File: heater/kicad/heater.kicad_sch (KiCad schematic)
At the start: 78 parts, among them J1 Conn_01x02_Pin, J2 Conn_01x02_Pin, J5 pcie_98, U1 OPA863DBVR, U10 B0509XT-1WR3, U14 OPA863DBVR, U15 LTC1968, U16 OPA863DBVR, U2 ESD5344D-TP, U4 TPS7A2050PDBVR, U5 ISO1541, U6 LTC1968, U7 OPA863DBVR, U8 ADS1115IDGS, U9 XC6206P332MR

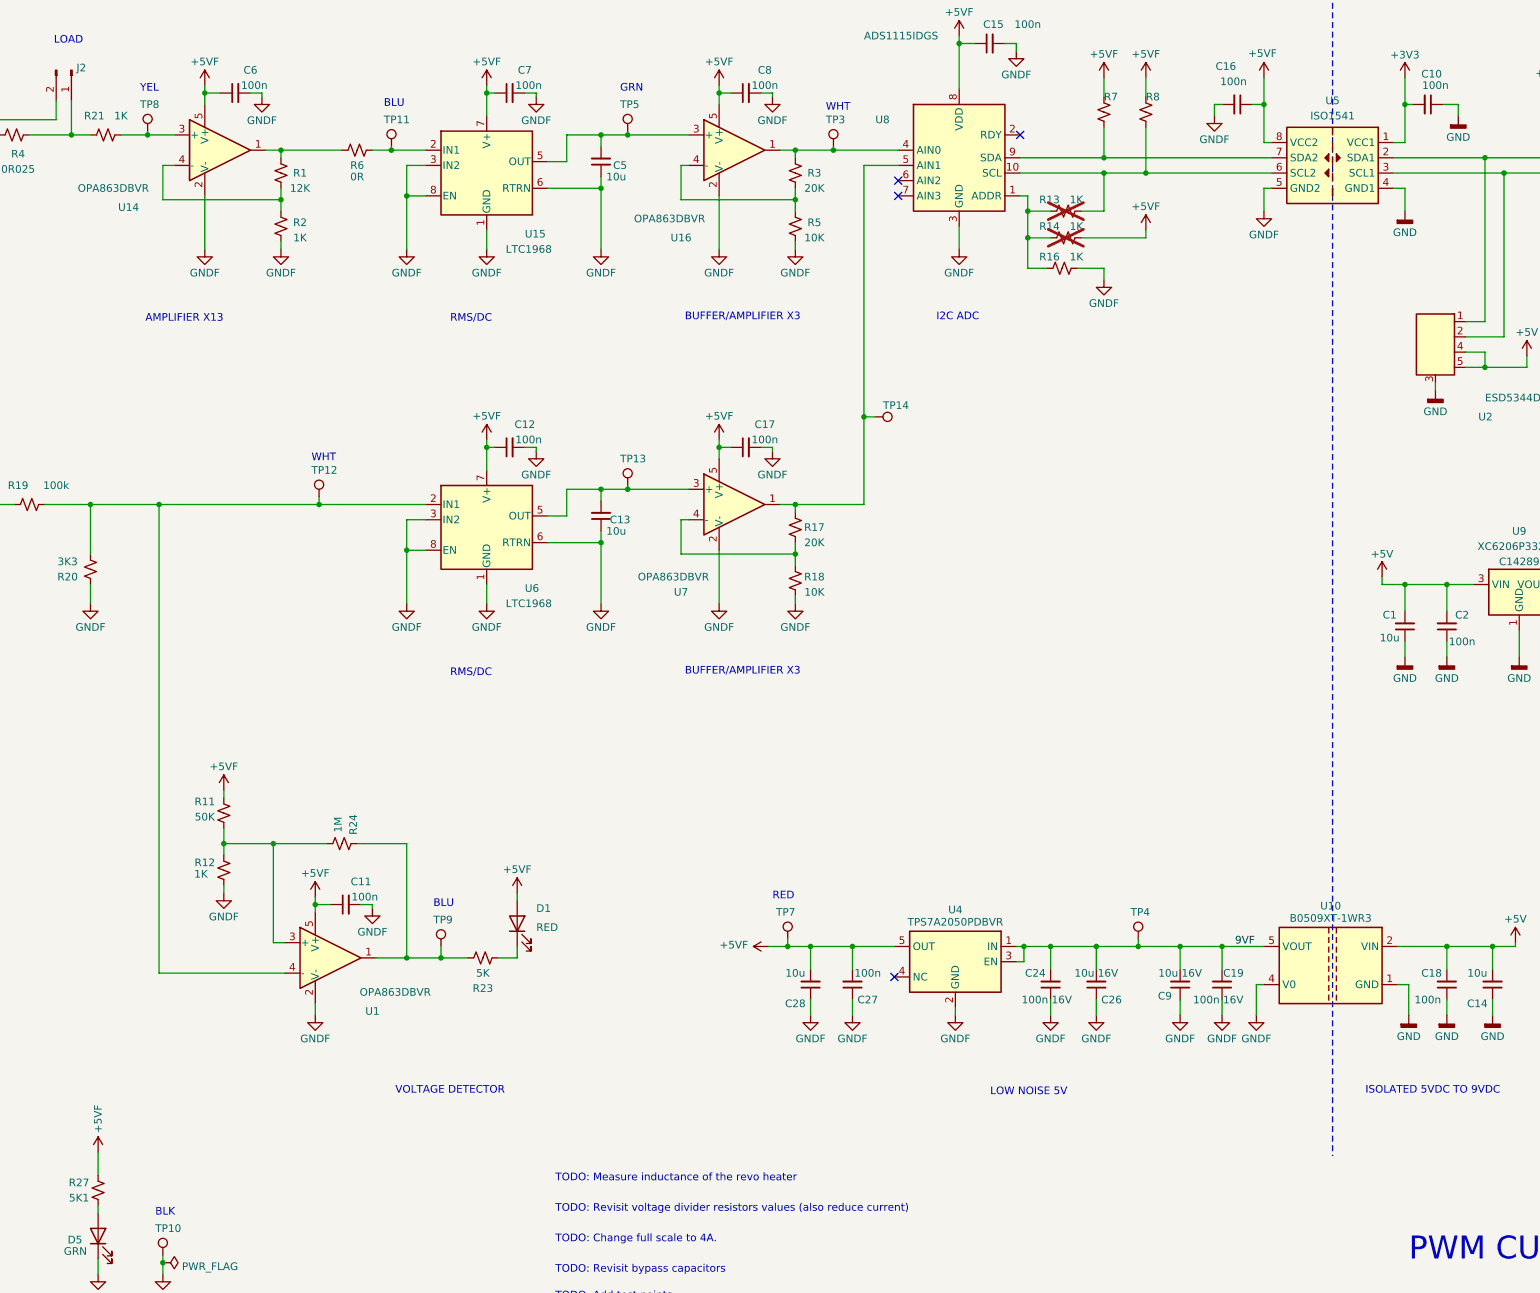
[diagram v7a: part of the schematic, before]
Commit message: Updated heater schematic.
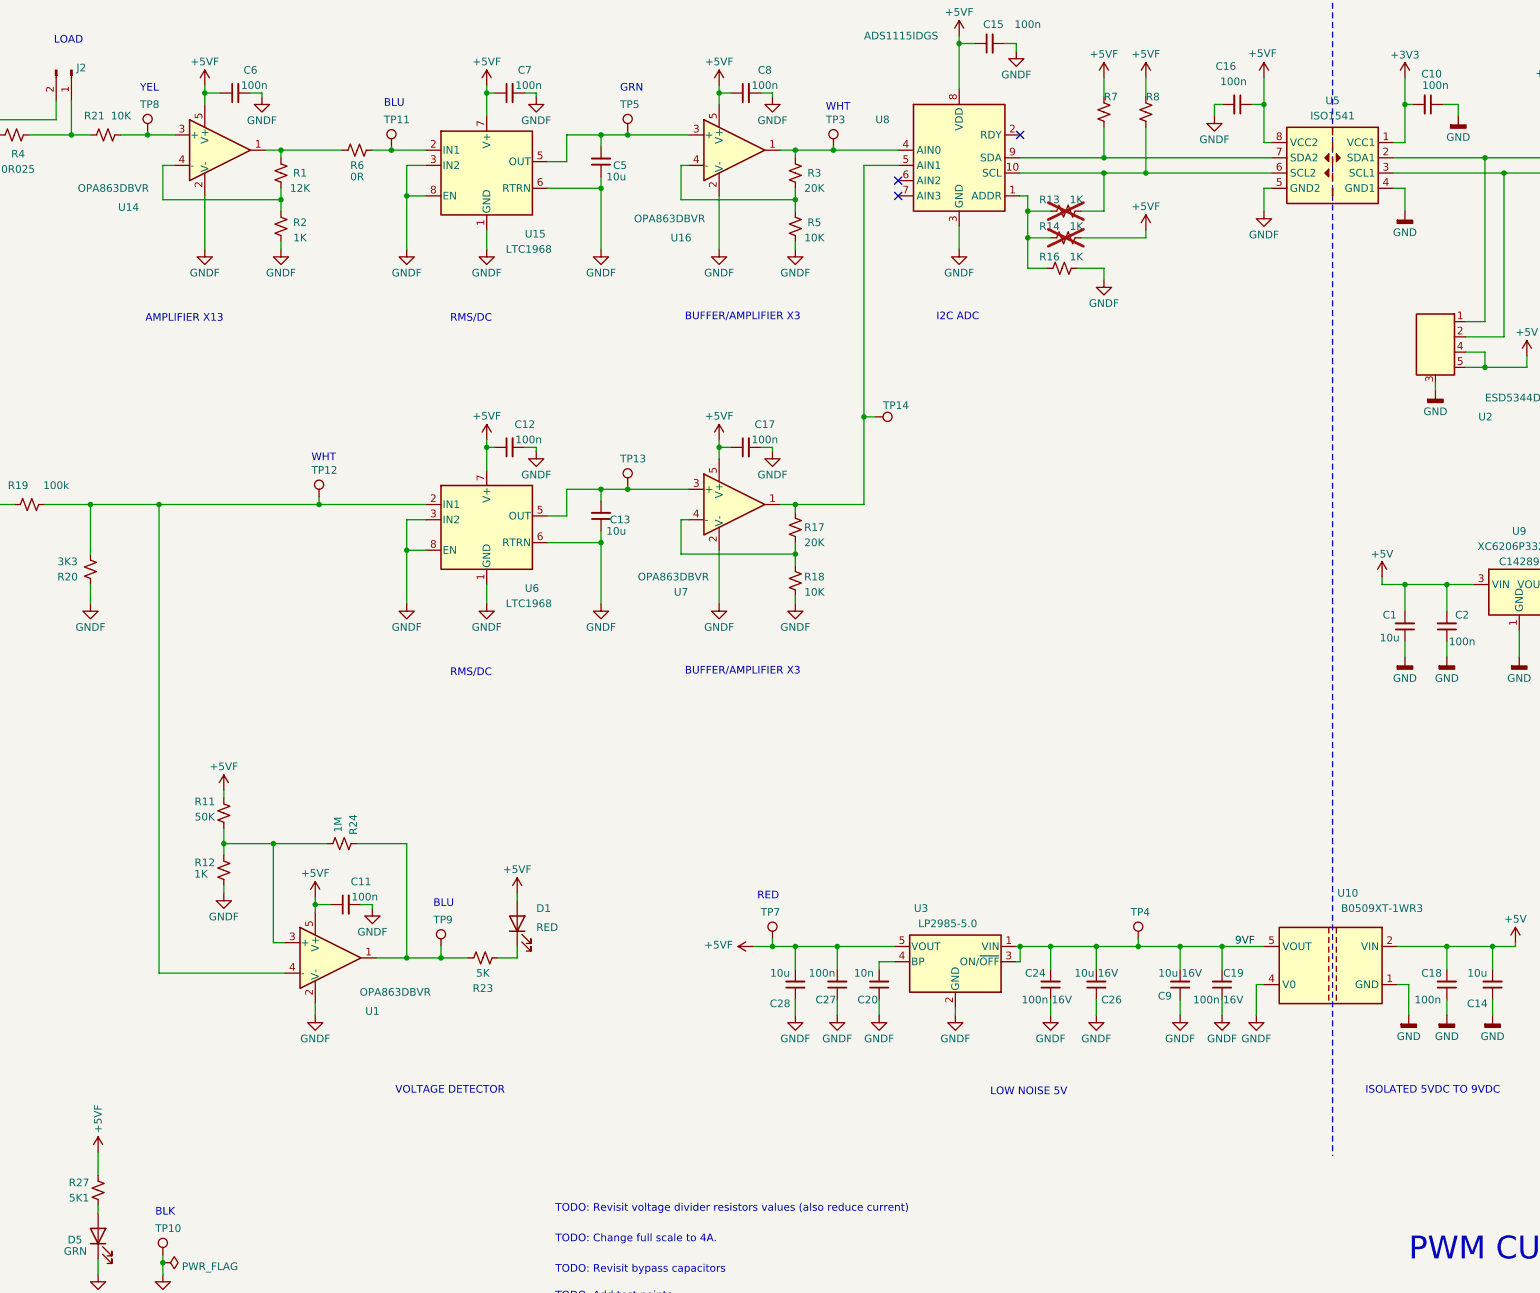
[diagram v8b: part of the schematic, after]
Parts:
- removed U4: TPS7A2050PDBVR, heater:SOT-23-5, symbol heater:TPS7A2050
- added C20: 10n, Capacitor_SMD:C_0402_1005Metric, symbol Device:C_Small
- added U3: LP2985-5.0, Package_TO_SOT_SMD:SOT-23-5, symbol Regulator_Linear:LP2985-5.0
- R21: value 1K -> 10K; LCSC C11702 -> (none)
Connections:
- net +5VF: now also U3.5 (VOUT)
- net 9VF: now also U3.1 (VIN), U3.3 (ON/~{OFF})
- net GND1: now also C20.1, U3.2 (GND)
- new net: C20.2, U3.4 (BP)
- no-connect marks 92 -> 91
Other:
- note removed: "TODO: Measure inductance of the revo heater"
- moved on the sheet: C27, C28, TP7
